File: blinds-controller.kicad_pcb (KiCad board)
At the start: 2 copper layers, 50 x 70 mm, 13 parts, among them J1 Jack-DC, J2 Stepper Motor, J3 DC Check, J4 JTAG, SW1 BOOT, U1 MPM3610AGQV-P, U2 ESP32-S2-WROOM, U3 ULN2003A

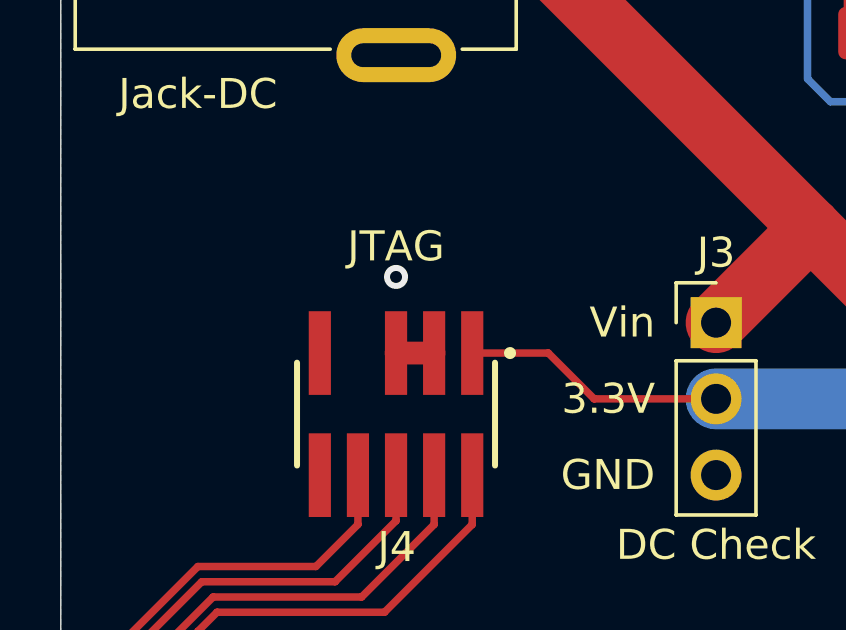
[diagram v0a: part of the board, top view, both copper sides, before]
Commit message: Connected JTAG GND
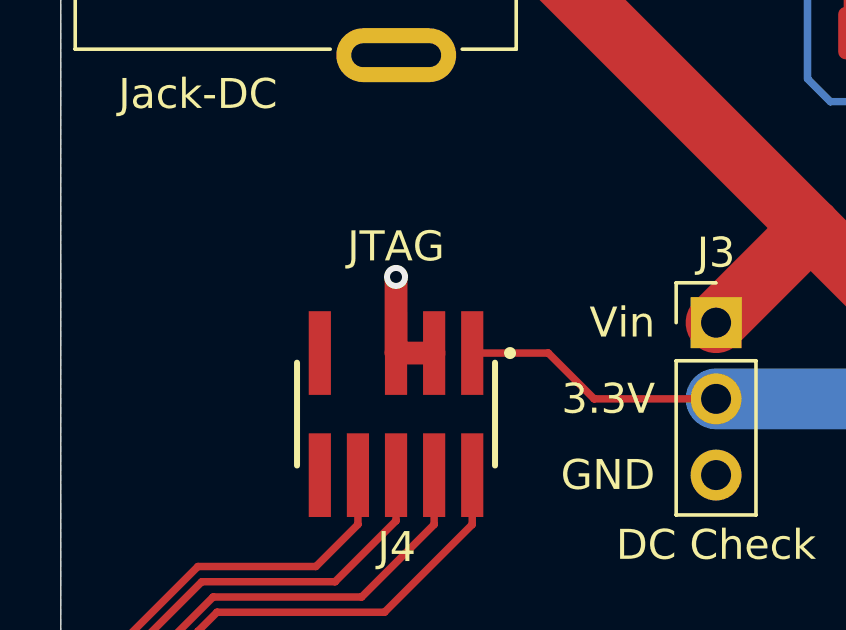
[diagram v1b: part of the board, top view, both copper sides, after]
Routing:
- net GND: track 31.5 -> 34.1 mm
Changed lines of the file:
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@@
     (thickness 1.6)
     (drawings 19)
-    (tracks 189)
+    (tracks 190)
     (zones 0)
     (modules 13)
@@
   )
   (setup
-    (last_trace_width 0.25)
+    (last_trace_width 0.76)
     (user_trace_width 0.76)
     (user_trace_width 2.03)
@@
   (segment (start 65.786 43.685) (end 64.516 43.685) (width 0.76) (layer F.Cu) (net 2))
   (via (at 64.516 41.148) (size 0.8) (drill 0.4) (layers F.Cu B.Cu) (net 2))
+  (segment (start 64.516 41.148) (end 64.516 43.685) (width 0.76) (layer F.Cu) (net 2))
   (segment (start 92.576 68.968) (end 90.932 70.612) (width 0.76) (layer F.Cu) (net 3))
   (segment (start 92.576 50.292) (end 92.576 68.968) (width 0.76) (layer F.Cu) (net 3))

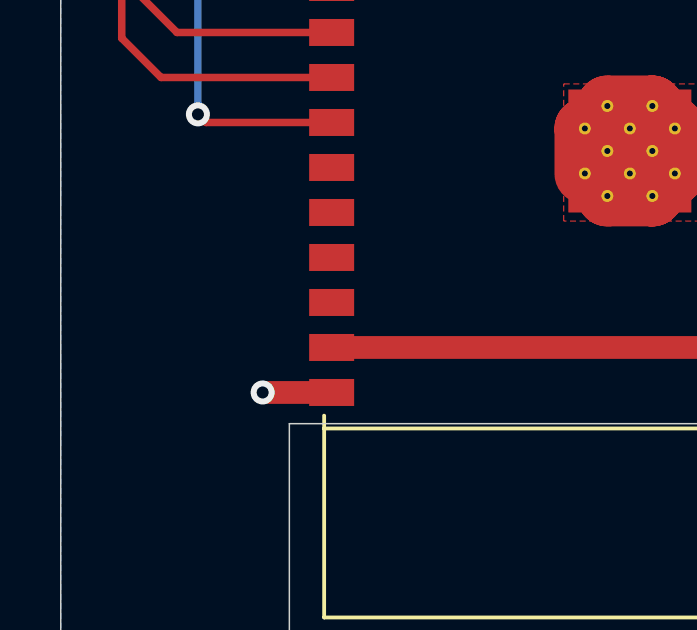
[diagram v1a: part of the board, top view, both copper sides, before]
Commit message: Added decoupling capacitors to ESP32
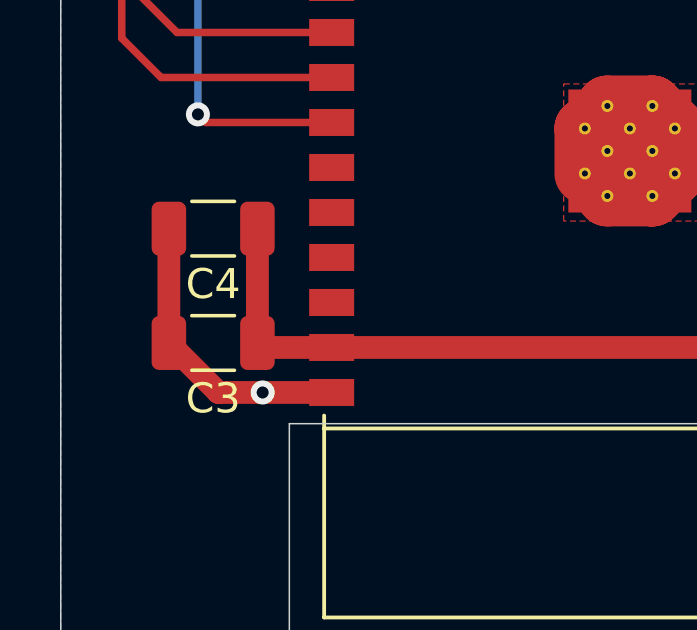
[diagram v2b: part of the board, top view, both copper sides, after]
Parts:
- added C3: 22uF, Capacitor_SMD:C_1206_3216Metric, F.Cu at (58.4, 78.7)
- added C4: 0.1uF, Capacitor_SMD:C_1206_3216Metric, F.Cu at (58.4, 74.9)
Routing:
- net GND: track 34.1 -> 41.2 mm
- net +3V3: track 113.5 -> 119.4 mm
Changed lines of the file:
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@@
     (thickness 1.6)
     (drawings 19)
-    (tracks 190)
+    (tracks 196)
     (zones 0)
-    (modules 13)
+    (modules 15)
     (nets 19)
   )
@@
     (add_net Stepper.D)
   )
+  (module Capacitor_SMD:C_1206_3216Metric (layer F.Cu)
+    (at 58.42 74.93 180)
+    (descr "Capacitor SMD 1206 (3216 Metric), square (rectangular) end terminal, IPC_7351 nominal, (Body size source: IPC-SM-782 page 76, https://www.pcb-3d.com/wordpress/wp-content/uploads/ipc-sm-782a_amendment_1_and_2.pdf), generated with kicad-footprint-generator")
+    (tags capacitor)
+    (attr smd)
+    (fp_text reference C4 (at 0 -1.85) (layer F.SilkS)
+      (effects (font (size 1 1) (thickness 0.15)))
+    )
+    (fp_text value 0.1uF (at 0 1.85) (layer F.Fab)
+      (effects (font (size 1 1) (thickness 0.15)))
+    )
+    (fp_text user %R (at 0 0) (layer F.Fab)
+      (effects (font (size 0.8 0.8) (thickness 0.12)))
+    )
+    (fp_line (start -1.6 0.8) (end -1.6 -0.8) (layer F.Fab) (width 0.1))
+    (fp_line (start -1.6 -0.8) (end 1.6 -0.8) (layer F.Fab) (width 0.1))
+    (fp_line (start 1.6 -0.8) (end 1.6 0.8) (layer F.Fab) (width 0.1))
+    (fp_line (start 1.6 0.8) (end -1.6 0.8) (layer F.Fab) (width 0.1))
+    (fp_line (start -0.711252 -0.91) (end 0.711252 -0.91) (layer F.SilkS) (width 0.12))
+    (fp_line (start -0.711252 0.91) (end 0.711252 0.91) (layer F.SilkS) (width 0.12))
+    (fp_line (start -2.3 1.15) (end -2.3 -1.15) (layer F.CrtYd) (width 0.05))
+    (fp_line (start -2.3 -1.15) (end 2.3 -1.15) (layer F.CrtYd) (width 0.05))
+    (fp_line (start 2.3 -1.15) (end 2.3 1.15) (layer F.CrtYd) (width 0.05))
+    (fp_line (start 2.3 1.15) (end -2.3 1.15) (layer F.CrtYd) (width 0.05))
+    (pad 2 smd roundrect (at 1.475 0 180) (size 1.15 1.8) (layers F.Cu F.Paste F.Mask) (roundrect_rratio 0.217391)
+      (net 2 GND))
+    (pad 1 smd roundrect (at -1.475 0 180) (size 1.15 1.8) (layers F.Cu F.Paste F.Mask) (roundrect_rratio 0.217391)
+      (net 11 +3V3))
+    (model ${KISYS3DMOD}/Capacitor_SMD.3dshapes/C_1206_3216Metric.wrl
+      (at (xyz 0 0 0))
+      (scale (xyz 1 1 1))
+      (rotate (xyz 0 0 0))
+    )
+  )
+  (module Capacitor_SMD:C_1206_3216Metric (layer F.Cu)
+    (at 58.42 78.74 180)
+    (descr "Capacitor SMD 1206 (3216 Metric), square (rectangular) end terminal, IPC_7351 nominal, (Body size source: IPC-SM-782 page 76, https://www.pcb-3d.com/wordpress/wp-content/uploads/ipc-sm-782a_amendment_1_and_2.pdf), generated with kicad-footprint-generator")
+    (tags capacitor)
+    (attr smd)
+    (fp_text reference C3 (at 0 -1.85) (layer F.SilkS)
+      (effects (font (size 1 1) (thickness 0.15)))
+    )
+    (fp_text value 22uF (at 0 1.85) (layer F.Fab)
+      (effects (font (size 1 1) (thickness 0.15)))
+    )
+    (fp_text user %R (at 0 0) (layer F.Fab)
+      (effects (font (size 0.8 0.8) (thickness 0.12)))
+    )
+    (fp_line (start -1.6 0.8) (end -1.6 -0.8) (layer F.Fab) (width 0.1))
+    (fp_line (start -1.6 -0.8) (end 1.6 -0.8) (layer F.Fab) (width 0.1))
+    (fp_line (start 1.6 -0.8) (end 1.6 0.8) (layer F.Fab) (width 0.1))
+    (fp_line (start 1.6 0.8) (end -1.6 0.8) (layer F.Fab) (width 0.1))
+    (fp_line (start -0.711252 -0.91) (end 0.711252 -0.91) (layer F.SilkS) (width 0.12))
+    (fp_line (start -0.711252 0.91) (end 0.711252 0.91) (layer F.SilkS) (width 0.12))
+    (fp_line (start -2.3 1.15) (end -2.3 -1.15) (layer F.CrtYd) (width 0.05))
+    (fp_line (start -2.3 -1.15) (end 2.3 -1.15) (layer F.CrtYd) (width 0.05))
+    (fp_line (start 2.3 -1.15) (end 2.3 1.15) (layer F.CrtYd) (width 0.05))
+    (fp_line (start 2.3 1.15) (end -2.3 1.15) (layer F.CrtYd) (width 0.05))
+    (pad 2 smd roundrect (at 1.475 0 180) (size 1.15 1.8) (layers F.Cu F.Paste F.Mask) (roundrect_rratio 0.217391)
+      (net 2 GND))
+    (pad 1 smd roundrect (at -1.475 0 180) (size 1.15 1.8) (layers F.Cu F.Paste F.Mask) (roundrect_rratio 0.217391)
+      (net 11 +3V3))
+    (model ${KISYS3DMOD}/Capacitor_SMD.3dshapes/C_1206_3216Metric.wrl
+      (at (xyz 0 0 0))
+      (scale (xyz 1 1 1))
+      (rotate (xyz 0 0 0))
+    )
+  )
   (module "footprints:PTS526 SM15 SMTR2 LFS" (layer F.Cu)
     (at 99.06 39.37)
@@
   (via (at 64.516 41.148) (size 0.8) (drill 0.4) (layers F.Cu B.Cu) (net 2))
   (segment (start 64.516 41.148) (end 64.516 43.685) (width 0.76) (layer F.Cu) (net 2))
+  (segment (start 56.945 75.39) (end 56.945 78.74) (width 0.76) (layer F.Cu) (net 2))
+  (segment (start 58.595 80.39) (end 60.07 80.39) (width 0.76) (layer F.Cu) (net 2))
+  (segment (start 56.945 78.74) (end 58.595 80.39) (width 0.76) (layer F.Cu) (net 2))
   (segment (start 92.576 68.968) (end 90.932 70.612) (width 0.76) (layer F.Cu) (net 3))
   (segment (start 92.576 50.292) (end 92.576 68.968) (width 0.76) (layer F.Cu) (net 3))
@@
   (segment (start 71.12 45.212) (end 75.184 45.212) (width 0.25) (layer F.Cu) (net 11))
   (segment (start 69.593 43.685) (end 71.12 45.212) (width 0.25) (layer F.Cu) (net 11))
+  (segment (start 60.045 78.89) (end 59.895 78.74) (width 0.76) (layer F.Cu) (net 11))
+  (segment (start 62.37 78.89) (end 60.045 78.89) (width 0.76) (layer F.Cu) (net 11))
+  (segment (start 59.895 78.74) (end 59.895 75.39) (width 0.76) (layer F.Cu) (net 11))
   (segment (start 80.01 30.6725) (end 80.282501 30.399999) (width 0.25) (layer F.Cu) (net 12))
   (segment (start 80.01 32.8275) (end 79.8175 33.02) (width 0.76) (layer F.Cu) (net 12))

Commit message: Added decoupling capacitors to ULN2003A
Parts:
- added C5: 10uF, Capacitor_SMD:C_1206_3216Metric, F.Cu at (87.0, 62.2)
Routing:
- net +12V: track 66.6 -> 70.6 mm
- net GND: track 41.2 -> 42.9 mm, vias 31 -> 32
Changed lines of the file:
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@@
     (thickness 1.6)
     (drawings 19)
-    (tracks 196)
+    (tracks 200)
     (zones 0)
-    (modules 15)
+    (modules 16)
     (nets 19)
   )
@@
   )
   (module Capacitor_SMD:C_1206_3216Metric (layer F.Cu)
+    (at 86.995 62.23 270)
+    (descr "Capacitor SMD 1206 (3216 Metric), square (rectangular) end terminal, IPC_7351 nominal, (Body size source: IPC-SM-782 page 76, https://www.pcb-3d.com/wordpress/wp-content/uploads/ipc-sm-782a_amendment_1_and_2.pdf), generated with kicad-footprint-generator")
+    (tags capacitor)
+    (attr smd)
+    (fp_text reference C5 (at 0 -1.85 90) (layer F.SilkS)
+      (effects (font (size 1 1) (thickness 0.15)))
+    )
+    (fp_text value 10uF (at 0 1.85 90) (layer F.Fab)
+      (effects (font (size 1 1) (thickness 0.15)))
+    )
+    (fp_text user %R (at 0 0 90) (layer F.Fab)
+      (effects (font (size 0.8 0.8) (thickness 0.12)))
+    )
+    (fp_line (start -1.6 0.8) (end -1.6 -0.8) (layer F.Fab) (width 0.1))
+    (fp_line (start -1.6 -0.8) (end 1.6 -0.8) (layer F.Fab) (width 0.1))
+    (fp_line (start 1.6 -0.8) (end 1.6 0.8) (layer F.Fab) (width 0.1))
+    (fp_line (start 1.6 0.8) (end -1.6 0.8) (layer F.Fab) (width 0.1))
+    (fp_line (start -0.711252 -0.91) (end 0.711252 -0.91) (layer F.SilkS) (width 0.12))
+    (fp_line (start -0.711252 0.91) (end 0.711252 0.91) (layer F.SilkS) (width 0.12))
+    (fp_line (start -2.3 1.15) (end -2.3 -1.15) (layer F.CrtYd) (width 0.05))
+    (fp_line (start -2.3 -1.15) (end 2.3 -1.15) (layer F.CrtYd) (width 0.05))
+    (fp_line (start 2.3 -1.15) (end 2.3 1.15) (layer F.CrtYd) (width 0.05))
+    (fp_line (start 2.3 1.15) (end -2.3 1.15) (layer F.CrtYd) (width 0.05))
+    (pad 2 smd roundrect (at 1.475 0 270) (size 1.15 1.8) (layers F.Cu F.Paste F.Mask) (roundrect_rratio 0.217391)
+      (net 2 GND))
+    (pad 1 smd roundrect (at -1.475 0 270) (size 1.15 1.8) (layers F.Cu F.Paste F.Mask) (roundrect_rratio 0.217391)
+      (net 1 +12V))
+    (model ${KISYS3DMOD}/Capacitor_SMD.3dshapes/C_1206_3216Metric.wrl
+      (at (xyz 0 0 0))
+      (scale (xyz 1 1 1))
+      (rotate (xyz 0 0 0))
+    )
+  )
+  (module Capacitor_SMD:C_1206_3216Metric (layer F.Cu)
     (at 58.42 74.93 180)
     (descr "Capacitor SMD 1206 (3216 Metric), square (rectangular) end terminal, IPC_7351 nominal, (Body size source: IPC-SM-782 page 76, https://www.pcb-3d.com/wordpress/wp-content/uploads/ipc-sm-782a_amendment_1_and_2.pdf), generated with kicad-footprint-generator")
@@
   (segment (start 67.776 28.956) (end 78.338 39.518) (width 2.03) (layer F.Cu) (net 1))
   (segment (start 67.522 28.956) (end 67.776 28.956) (width 2.03) (layer F.Cu) (net 1))
+  (segment (start 87.298 60.452) (end 86.995 60.755) (width 0.76) (layer F.Cu) (net 1))
+  (segment (start 90.932 60.452) (end 87.298 60.452) (width 0.76) (layer F.Cu) (net 1))
   (segment (start 85.11 31.5) (end 84.07 31.5) (width 0.25) (layer F.Cu) (net 2))
   (segment (start 84.11383 31.64867) (end 84.11383 31.543829) (width 0.76) (layer F.Cu) (net 2))
@@
   (segment (start 58.595 80.39) (end 60.07 80.39) (width 0.76) (layer F.Cu) (net 2))
   (segment (start 56.945 78.74) (end 58.595 80.39) (width 0.76) (layer F.Cu) (net 2))
+  (via (at 86.995 65.405) (size 0.8) (drill 0.4) (layers F.Cu B.Cu) (net 2))
+  (segment (start 86.995 63.705) (end 86.995 65.405) (width 0.76) (layer F.Cu) (net 2))
   (segment (start 92.576 68.968) (end 90.932 70.612) (width 0.76) (layer F.Cu) (net 3))
   (segment (start 92.576 50.292) (end 92.576 68.968) (width 0.76) (layer F.Cu) (net 3))

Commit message: Added RESET switch and made some adjustments
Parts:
- added C6: 1uf, Capacitor_SMD:C_1206_3216Metric, F.Cu at (58.4, 77.9)
- added R4: 10k, Resistor_SMD:R_1206_3216Metric, F.Cu at (55.9, 73.7)
- SW1: value BOOT -> RESET
- moved SW1 60.4 mm to (57.8, 83.4), turned to 270 degrees
- moved C3 28.0 mm to (85.7, 85.1)
- moved C4 28.0 mm to (85.7, 81.3)
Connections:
- SW1 pad 1: (no net) -> RESET
- SW1 pad 2: (no net) -> RESET
- SW1 pad 3: (no net) -> GND
- SW1 pad 4: (no net) -> GND
- U2 pad 41: +3V3 -> RESET
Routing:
- net GND: track 42.9 -> 65.7 mm
- net +3V3: track 119.4 -> 134.9 mm, vias 20 -> 22
- net RESET: track 0.00 -> 13.7 mm
- net Net-(U1-Pad19): track 0.00 -> 2.15 mm

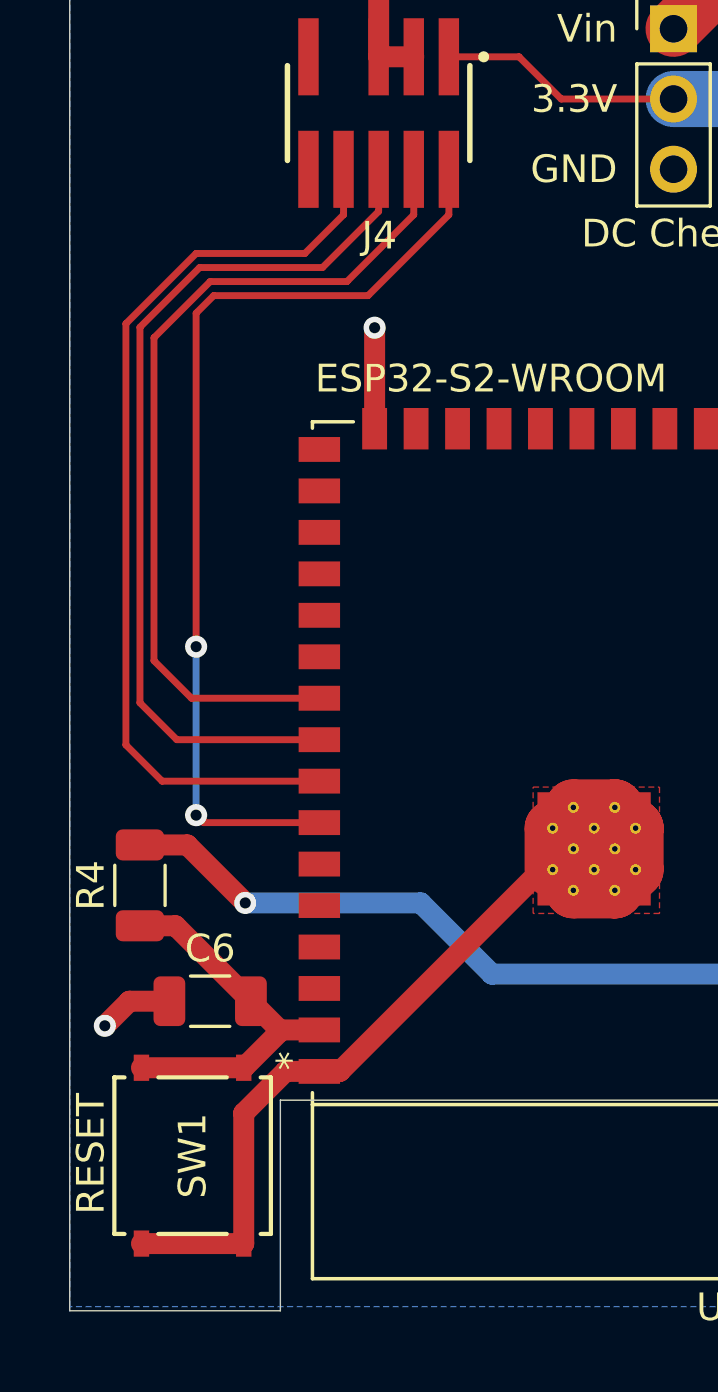
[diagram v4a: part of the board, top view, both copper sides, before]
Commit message: Opened up room for screw holes
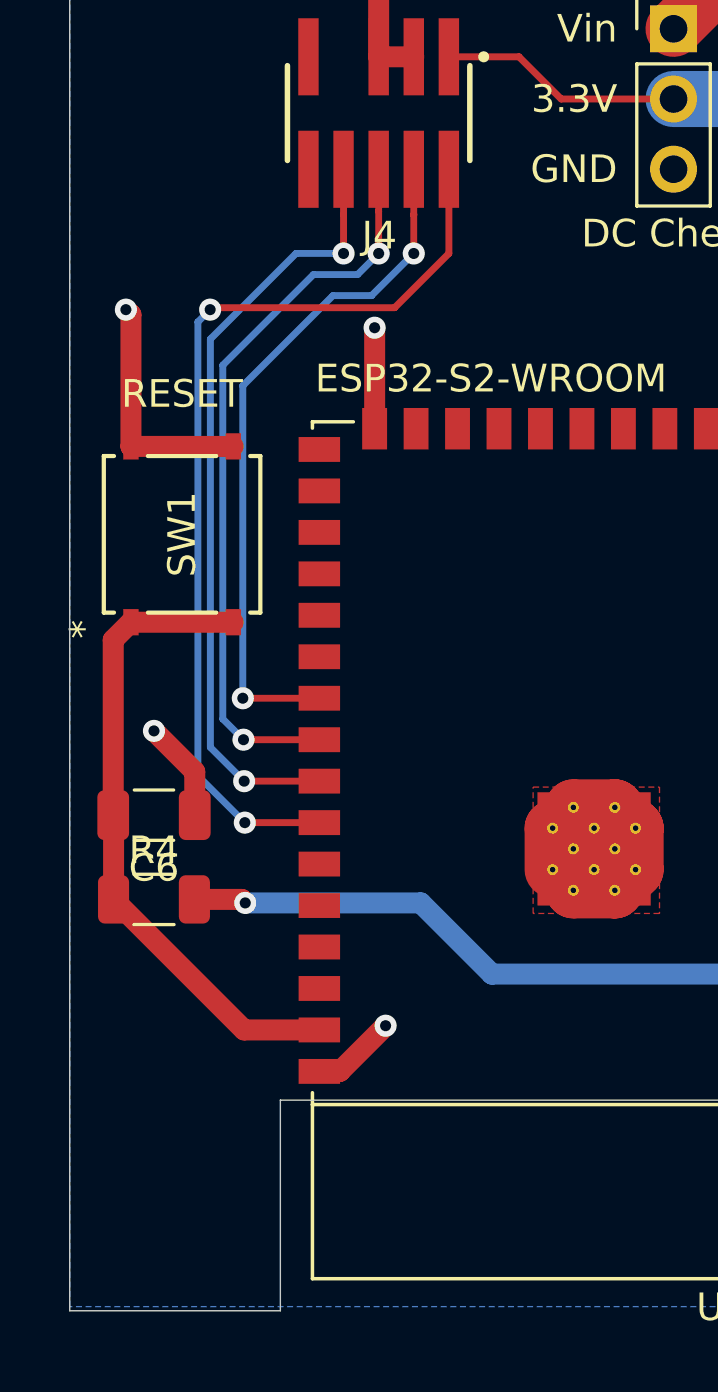
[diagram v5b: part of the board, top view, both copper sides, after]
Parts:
- moved SW1 22.5 mm to (57.4, 61.0), turned to 90 degrees
- moved C6 7.03 mm to (56.4, 71.1), turned to 0 degrees
- moved R4 0.72 mm to (56.4, 74.2), turned to 180 degrees
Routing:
- net GND: track 65.7 -> 55.6 mm, vias 32 -> 34
- net RESET: track 13.7 -> 23.4 mm
- net JTAG.TCK: track 31.1 -> 25.3 mm, vias 0 -> 2
- net JTAG.TDI: track 33.9 -> 28.4 mm, vias 0 -> 2
- net JTAG.TDO: track 32.5 -> 27.0 mm, vias 0 -> 2
- net +3V3: track 134.9 -> 132.1 mm
